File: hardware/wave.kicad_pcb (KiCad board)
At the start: 4 copper layers, 60 x 60 mm, 123 parts, among them J101 WAGO 2065-100, J102 WAGO 2065-100, J103 Cortex, J104 WAGO 2065-100, J105 WAGO 2065-100, J106 WAGO 2065-100, J107 WAGO 2065-100, J301 2x05_Horizontal, J401 2x05_Horizontal, J501 WAGO 2065-100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

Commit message: Refresh
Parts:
- U201: footprint V2_Package_DFN_QFN:QFN-64-1EP_9x9mm_P0.5mm_EP5.45x5.45mm_ThermalVias -> V2_Package_DFN_QFN:QFN-64-1EP_9x9mm_P0.5mm_EP6x6mm_ThermalVias

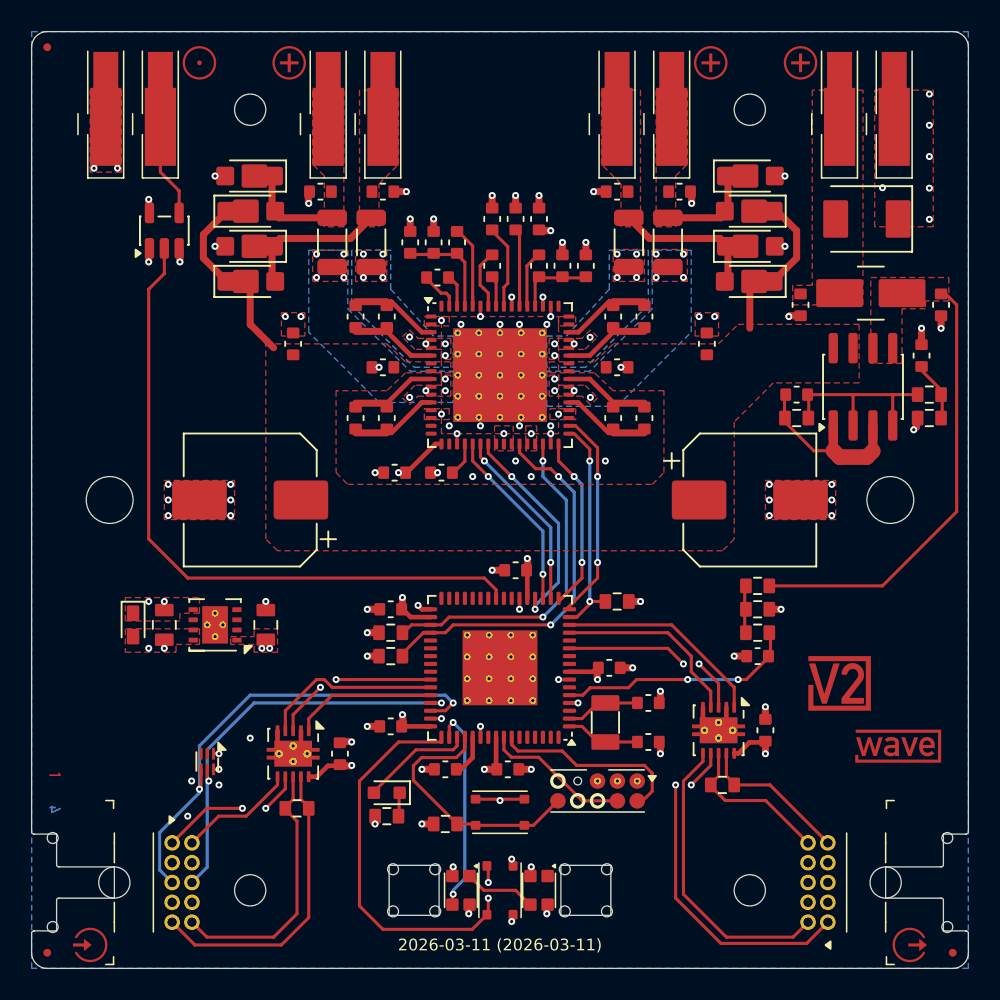
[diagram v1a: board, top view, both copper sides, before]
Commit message: Update ESD suppressor
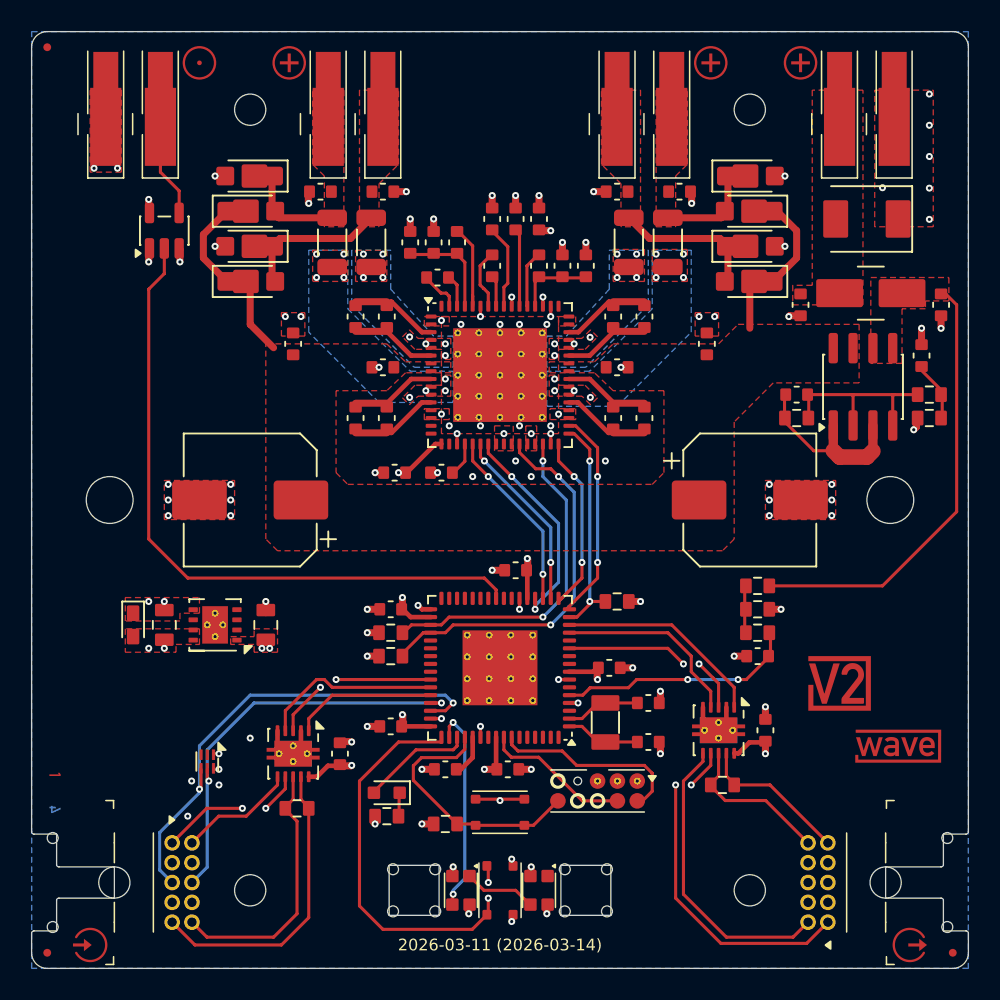
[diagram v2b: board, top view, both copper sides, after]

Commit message: Refresh
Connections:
- net /VDDCORE renamed /+VDDCORE

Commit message: Update
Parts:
- FB101: value 47 Ω -> 47Ω
- FB201, FB202, FB203, FB204: value 50 Ω -> 50Ω

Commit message: Update
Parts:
- renumbered C107 to C106, C106 to C107
